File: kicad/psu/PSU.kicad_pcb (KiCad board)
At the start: 2 copper layers, 54.5 x 47.7 mm, 0 parts

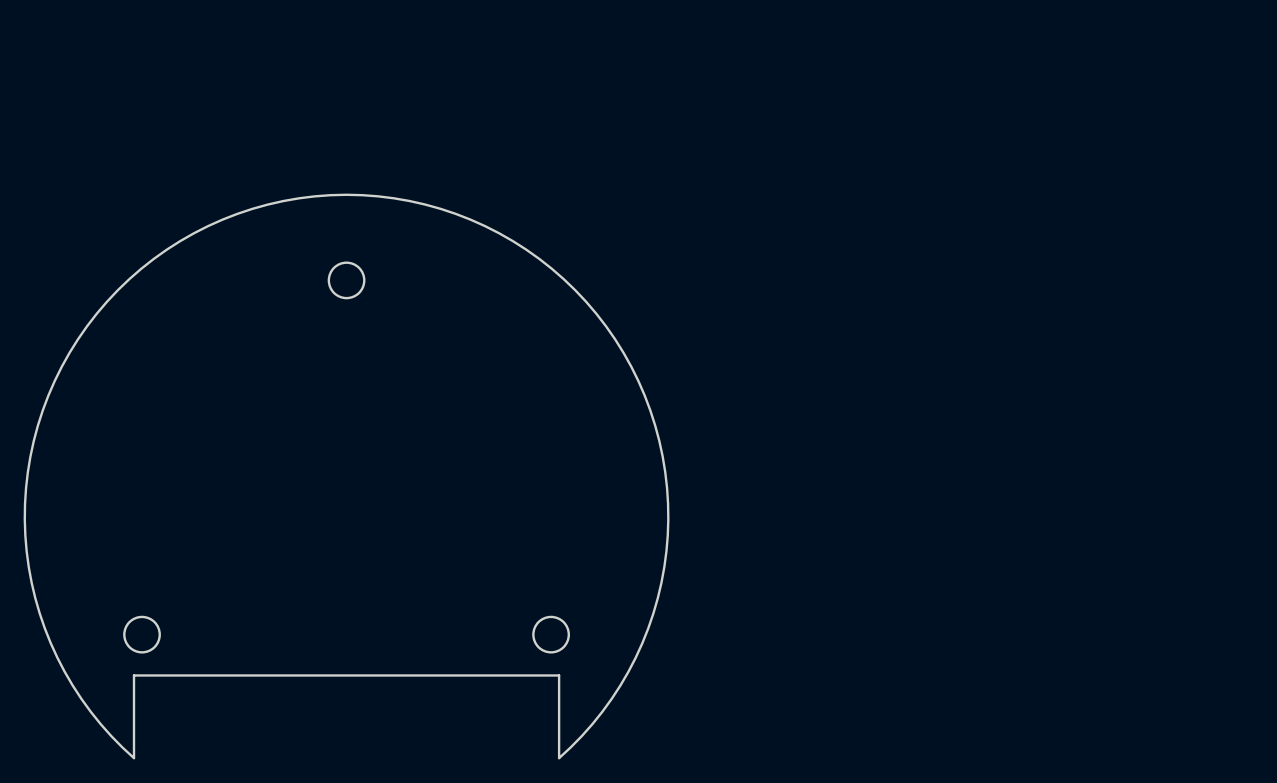
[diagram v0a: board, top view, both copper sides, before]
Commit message: Kicad(psu): changed the connector and usb-c to different psu footprints
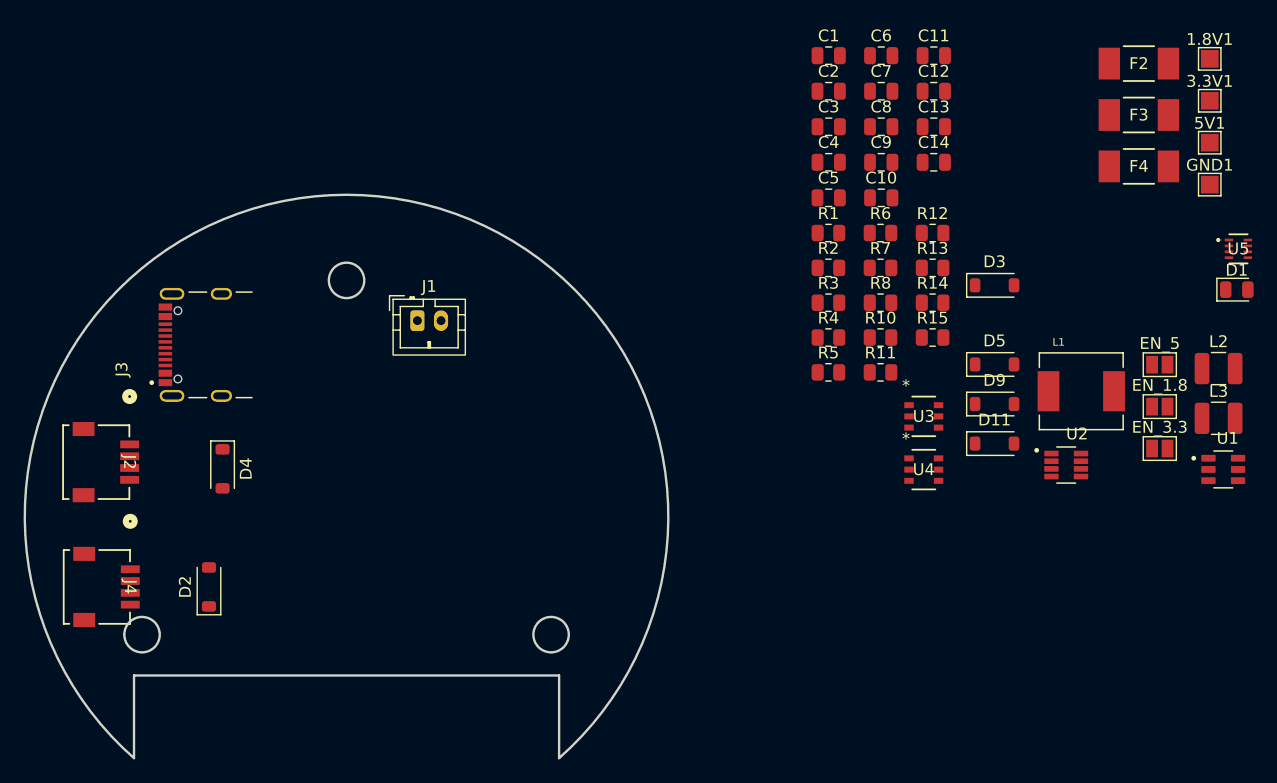
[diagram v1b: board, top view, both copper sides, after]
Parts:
- added 1.8V1: TestPoint, TestPoint:TestPoint_Pad_1.5x1.5mm, F.Cu at (272.1, 36.3)
- added 3.3V1: TestPoint, TestPoint:TestPoint_Pad_1.5x1.5mm, F.Cu at (272.1, 39.8)
- added 5V1: TestPoint, TestPoint:TestPoint_Pad_1.5x1.5mm, F.Cu at (272.1, 43.4)
- added C1: 22uF, Capacitor_SMD:C_0805_2012Metric, F.Cu at (239.8, 36.0)
- added C10: 22uF, Capacitor_SMD:C_0805_2012Metric, F.Cu at (244.3, 48.0)
- added C11: 22pF, Capacitor_SMD:C_0805_2012Metric, F.Cu at (248.7, 36.0)
- added C12: 22pF, Capacitor_SMD:C_0805_2012Metric, F.Cu at (248.7, 39.0)
- added C13: 22uF, Capacitor_SMD:C_0805_2012Metric, F.Cu at (248.7, 42.0)
- added C14: 22uF, Capacitor_SMD:C_0805_2012Metric, F.Cu at (248.7, 45.0)
- added C2: 2.2uF, Capacitor_SMD:C_0805_2012Metric, F.Cu at (239.8, 39.0)
- added C3: 22uF, Capacitor_SMD:C_0805_2012Metric, F.Cu at (239.8, 42.0)
- added C4: 2.2uF, Capacitor_SMD:C_0805_2012Metric, F.Cu at (239.8, 45.0)
- added C5: 22uF, Capacitor_SMD:C_0805_2012Metric, F.Cu at (239.8, 48.0)
- added C6: 22uF, Capacitor_SMD:C_0805_2012Metric, F.Cu at (244.3, 36.0)
- added C7: 22uF, Capacitor_SMD:C_0805_2012Metric, F.Cu at (244.3, 39.0)
- added C8: 22uF, Capacitor_SMD:C_0805_2012Metric, F.Cu at (244.3, 42.0)
- added C9: 22uF, Capacitor_SMD:C_0805_2012Metric, F.Cu at (244.3, 45.0)
- added D1: Green, LED_SMD:LED_0805_2012Metric, F.Cu at (274.4, 55.8)
- added D11: D_Schottky, Diode_SMD:D_SOD-123, F.Cu at (253.9, 68.9)
- added D2: D_Schottky, Diode_SMD:D_SOD-123, F.Cu at (187.3, 81.0)
- added D3: D_Schottky, Diode_SMD:D_SOD-123, F.Cu at (253.9, 55.5)
- added D4: D_Schottky, Diode_SMD:D_SOD-123, F.Cu at (188.5, 71.0)
- added D5: D_Schottky, Diode_SMD:D_SOD-123, F.Cu at (253.9, 62.2)
- added D9: D_Schottky, Diode_SMD:D_SOD-123, F.Cu at (253.9, 65.5)
- added EN_1.8: EN_1.8, Jumper:SolderJumper-2_P1.3mm_Open_Pad1.0x1.5mm, F.Cu at (267.9, 65.7)
- added EN_3.3: EN_3.3, Jumper:SolderJumper-2_P1.3mm_Open_Pad1.0x1.5mm, F.Cu at (267.9, 69.3)
- added EN_5: EN_5, Jumper:SolderJumper-2_P1.3mm_Open_Pad1.0x1.5mm, F.Cu at (267.9, 62.2)
- added F2: 1.5A, Fuses:0451Series_LTF, F.Cu at (266.1, 36.7)
- added F3: 1.5A, Fuses:0451Series_LTF, F.Cu at (266.1, 41.0)
- added F4: 1.5A, Fuses:0451Series_LTF, F.Cu at (266.1, 45.4)
- added GND1: TestPoint, TestPoint:TestPoint_Pad_1.5x1.5mm, F.Cu at (272.1, 46.9)
- added J1: B2B-PH-K-S, Connector_JST:JST_PH_B2B-PH-K_1x02_P2.00mm_Vertical, F.Cu at (205.0, 58.5)
- added J2: 5015680407, footprints:CONN_5015680000-SD_04_MOL, F.Cu at (177.8, 70.4)
- added J3: UJ20-C-H-G-SMT-1-P16-TR, footprints:SAMESKY_UJ20-C-H-G-SMT-1-P16-TR, F.Cu at (191.0, 60.5)
- added J4: 5015680407, footprints:CONN_5015680000-SD_04_MOL, F.Cu at (177.9, 81.0)
- added L1: 1u5H, PSAT_Library:IND_SPM6530T-1R5M100, F.Cu at (261.2, 64.4)
- added L2: 2u2H, Inductor_SMD:L_1210_3225Metric, F.Cu at (272.9, 62.5)
- added L3: 2u2H, Inductor_SMD:L_1210_3225Metric, F.Cu at (272.9, 66.7)
- added R1: 560, Resistor_SMD:R_0805_2012Metric, F.Cu at (239.8, 51.0)
- added R10: 1k5, Resistor_SMD:R_0805_2012Metric, F.Cu at (244.2, 59.9)
- added R11: 1Meg, Resistor_SMD:R_0805_2012Metric, F.Cu at (244.2, 62.8)
- added R12: 115K, Resistor_SMD:R_0805_2012Metric, F.Cu at (248.6, 51.0)
- added R13: 200K, Resistor_SMD:R_0805_2012Metric, F.Cu at (248.6, 54.0)
- added R14: 25.5K, Resistor_SMD:R_0805_2012Metric, F.Cu at (248.6, 56.9)
- added R15: 100K, Resistor_SMD:R_0805_2012Metric, F.Cu at (248.6, 59.9)
- added R2: 1Meg, Resistor_SMD:R_0805_2012Metric, F.Cu at (239.8, 54.0)
- added R3: 10K, Resistor_SMD:R_0805_2012Metric, F.Cu at (239.8, 56.9)
- added R4: 1Meg, Resistor_SMD:R_0805_2012Metric, F.Cu at (239.8, 59.9)
- added R5: 1K5, Resistor_SMD:R_0805_2012Metric, F.Cu at (239.8, 62.8)
- added R6: 30K, Resistor_SMD:R_0805_2012Metric, F.Cu at (244.2, 51.0)
- added R7: 270K, Resistor_SMD:R_0805_2012Metric, F.Cu at (244.2, 54.0)
- added R8: 22K, Resistor_SMD:R_0805_2012Metric, F.Cu at (244.2, 56.9)
- added U1: BQ21040DBVR, PSAT_Library:BQ21040DBVR, F.Cu at (273.2, 71.0)
- added U2: RT4812GJ8F, PSAT_Library:RT4812GJ8F, F.Cu at (259.9, 70.7)
- added U3: AP3445LW6-7, PSAT_Library:SOT26_AP3445_DIO-L, F.Cu at (247.9, 66.6)
- added U4: AP3445LW6-7, PSAT_Library:SOT26_AP3445_DIO-L, F.Cu at (247.9, 71.1)
- added U5: LM66200DRLR, footprints:SOT-5X3_DRL_TEX, F.Cu at (274.5, 52.4)
